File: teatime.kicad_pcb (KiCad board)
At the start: 2 copper layers, 100 x 100 mm, 90 parts, among them J1 PROG, Q1 2N7000, SW1 SW_Push, U1 MCP1700-3302E, U2 74HC595, U3 74HC595, U4 74HC595, U5 74HC595, U6 ATtiny85-20PU

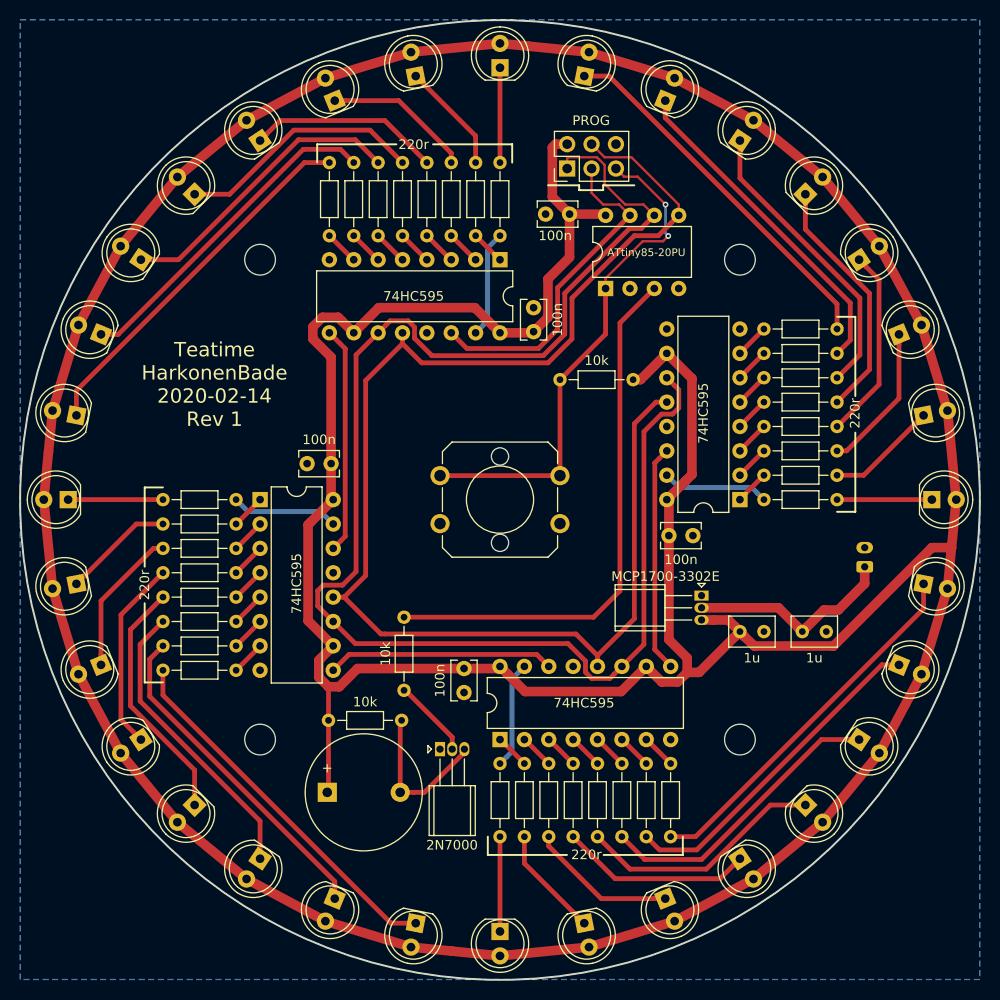
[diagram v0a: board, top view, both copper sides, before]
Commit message: SMD variant board
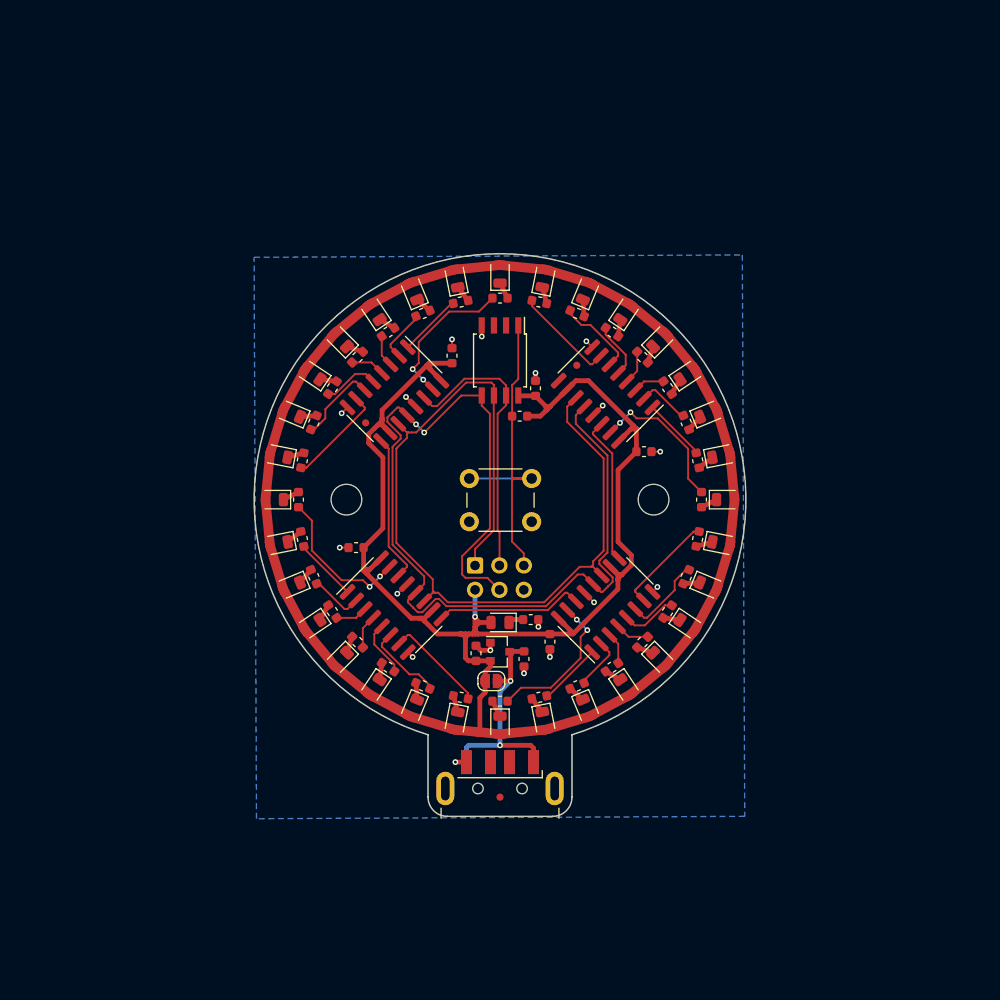
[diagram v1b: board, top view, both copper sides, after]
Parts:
- removed BT1: Battery_Cell, Connector_JST:JST_PH_S2B-PH-K_1x02_P2.00mm_Horizontal
- removed H3, H4: MountingHole, MountingHole:MountingHole_3.2mm_M3
- removed LS1: Speaker, Buzzer_Beeper:Buzzer_12x9.5RM7.6
- removed Q1: 2N7000, Package_TO_SOT_THT:TO-92_Inline_W4.0mm_Horizontal_FlatSideDown
- removed R34: 10k, Resistor_THT:R_Axial_DIN0204_L3.6mm_D1.6mm_P7.62mm_Horizontal
- removed the U3 at (75.0, 100.0)
- added D33: PWR, LED_SMD:LED_0805_2012Metric, F.Cu at (100.0, 112.8)
- added FID1: Fiducial, Fiducial:Fiducial_0.75mm_Mask1.5mm, F.Cu at (100.0, 131.0)
- added FID2: Fiducial, Fiducial:Fiducial_0.75mm_Mask1.5mm, F.Cu at (86.0, 92.0)
- added FID3: Fiducial, Fiducial:Fiducial_0.75mm_Mask1.5mm, F.Cu at (108.0, 86.0)
- added J2: PROG, Connector_IDC:IDC-Header_2x03_P2.54mm_Vertical, B.Cu at (97.4, 106.9)
- added JP1: SolderJumper_2_Open, Jumper:SolderJumper-2_P1.3mm_Open_RoundedPad1.0x1.5mm, F.Cu at (99.1, 118.9)
- added U2: 74HC595, Package_SO:SOIC-16_3.9x9.9mm_P1.27mm, F.Cu at (89.0, 89.0)
- C1, C2: footprint Capacitor_THT:C_Rect_L4.6mm_W3.0mm_P2.50mm_MKS02_FKP02 -> Resistor_SMD:R_0603_1608Metric
- C3, C4, C5, C6, C7: footprint Capacitor_THT:C_Rect_L4.0mm_W2.5mm_P2.50mm -> Resistor_SMD:R_0603_1608Metric
- D1, D10, D11, D12, D13, D14, D15, D16, D17, D18, D19, D2, D20, D21, D22, D23, D24, D25, D26, D27, D28, D29, D3, D30, D31, D32, D4, D5, D6, D7, D8, D9: footprint LED_THT:LED_D5.0mm -> LED_SMD:LED_0805_2012Metric
- J1: value PROG -> USB_A; footprint Connector_PinHeader_2.54mm:PinHeader_2x03_P2.54mm_Vertical -> teatime:USB_A_CNCTech_1001-011-01101_Horizontal_DoubleSided
- R1, R10, R11, R12, R13, R14, R15, R16, R17, R18, R19, R2, R20, R21, R22, R23, R24, R25, R26, R27, R28, R29, R3, R30, R31, R32, R4, R5, R6, R7, R8, R9: value 220r -> 1k; footprint Resistor_THT:R_Axial_DIN0204_L3.6mm_D1.6mm_P7.62mm_Horizontal -> Resistor_SMD:R_0603_1608Metric
- R33: value 10k -> 2k2; footprint Resistor_THT:R_Axial_DIN0204_L3.6mm_D1.6mm_P7.62mm_Horizontal -> Resistor_SMD:R_0603_1608Metric
- R35: footprint Resistor_THT:R_Axial_DIN0204_L3.6mm_D1.6mm_P7.62mm_Horizontal -> Resistor_SMD:R_0603_1608Metric
- SW1: footprint teatime:B3F-40xx -> Button_Switch_THT:SW_PUSH_6mm
- U1: value MCP1700-3302E -> MCP1700-3302E_SOT23; footprint Package_TO_SOT_THT:TO-92_Inline_W4.0mm_Horizontal_FlatSideDown -> Package_TO_SOT_SMD:SOT-23
- U3: renamed from U2; value 74HC595 -> ATtiny45-20SU; footprint Package_DIP:DIP-16_W7.62mm -> Package_SO:SOIJ-8_5.3x5.3mm_P1.27mm
- U4, U5: footprint Package_DIP:DIP-16_W7.62mm -> Package_SO:SOIC-16_3.9x9.9mm_P1.27mm
- U6: value ATtiny85-20PU -> 74HC595; footprint Package_DIP:DIP-8_W7.62mm -> Package_SO:SOIC-16_3.9x9.9mm_P1.27mm
- moved J1 71.8 mm to (100.0, 137.0), turned to 270 degrees
- moved C5 32.6 mm to (115.0, 95.0), turned to 0 degrees
- moved HS1 30.0 mm to (100.0, 86.0)
- moved C1 29.1 mm to (102.5, 116.6), turned to 270 degrees
- moved C4 29.1 mm to (85.0, 105.0), turned to 180 degrees
- moved C2 27.6 mm to (97.5, 116.0), turned to 90 degrees
- moved H1 26.6 mm to (84.0, 100.0)
- moved H2 26.6 mm to (116.0, 100.0)
- moved R33 25.2 mm to (103.2, 112.5)
- moved R35 24.2 mm to (102.0, 91.3), turned to 0 degrees
- moved R32 23.6 mm to (104.1, 79.4), turned to 168.75 degrees
- moved R24 23.6 mm to (120.6, 104.1), turned to 78.75 degrees
- moved R8 23.6 mm to (79.4, 95.9), turned to 258.75 degrees
- moved R16 23.6 mm to (95.9, 120.6), turned to 348.75 degrees
- moved U1 21.8 mm to (100.0, 115.8), turned to 0 degrees
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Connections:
- C1 pad 1: Net-(BT1-Pad1) -> Net-(C1-Pad1)
- J1 pad 1: Net-(J1-Pad1) -> Net-(C1-Pad1)
- J1 pad 2: +3V3 -> Net-(J1-Pad2)
- J1 pad 4: Net-(J1-Pad4) -> GND
- J1 pad 5: Net-(J1-Pad5) -> GND
- R1 pad 1: Net-(R1-Pad1) -> Net-(D1-Pad1)
- R1 pad 2: Net-(D1-Pad1) -> Net-(R1-Pad2)
- R10 pad 1: Net-(R10-Pad1) -> Net-(D10-Pad1)
- R10 pad 2: Net-(D10-Pad1) -> Net-(R10-Pad2)
- R11 pad 1: Net-(R11-Pad1) -> Net-(D11-Pad1)
- R11 pad 2: Net-(D11-Pad1) -> Net-(R11-Pad2)
- R12 pad 1: Net-(R12-Pad1) -> Net-(D12-Pad1)
- R12 pad 2: Net-(D12-Pad1) -> Net-(R12-Pad2)
- R13 pad 1: Net-(R13-Pad1) -> Net-(D13-Pad1)
- R13 pad 2: Net-(D13-Pad1) -> Net-(R13-Pad2)
- R14 pad 1: Net-(R14-Pad1) -> Net-(D14-Pad1)
- R14 pad 2: Net-(D14-Pad1) -> Net-(R14-Pad2)
- R15 pad 1: Net-(R15-Pad1) -> Net-(D15-Pad1)
- R15 pad 2: Net-(D15-Pad1) -> Net-(R15-Pad2)
- R16 pad 1: Net-(R16-Pad1) -> Net-(D16-Pad1)
- R16 pad 2: Net-(D16-Pad1) -> Net-(R16-Pad2)
- R17 pad 1: Net-(R17-Pad1) -> Net-(D17-Pad1)
- R17 pad 2: Net-(D17-Pad1) -> Net-(R17-Pad2)
- R18 pad 1: Net-(R18-Pad1) -> Net-(D18-Pad1)
- R18 pad 2: Net-(D18-Pad1) -> Net-(R18-Pad2)
- R19 pad 1: Net-(R19-Pad1) -> Net-(D19-Pad1)
- R19 pad 2: Net-(D19-Pad1) -> Net-(R19-Pad2)
- R2 pad 1: Net-(R2-Pad1) -> Net-(D2-Pad1)
- R2 pad 2: Net-(D2-Pad1) -> Net-(R2-Pad2)
- R20 pad 1: Net-(R20-Pad1) -> Net-(D20-Pad1)
- R20 pad 2: Net-(D20-Pad1) -> Net-(R20-Pad2)
- R21 pad 1: Net-(R21-Pad1) -> Net-(D21-Pad1)
- R21 pad 2: Net-(D21-Pad1) -> Net-(R21-Pad2)
- R22 pad 1: Net-(R22-Pad1) -> Net-(D22-Pad1)
- R22 pad 2: Net-(D22-Pad1) -> Net-(R22-Pad2)
- R23 pad 1: Net-(R23-Pad1) -> Net-(D23-Pad1)
- R23 pad 2: Net-(D23-Pad1) -> Net-(R23-Pad2)
- R24 pad 1: Net-(R24-Pad1) -> Net-(D24-Pad1)
- R24 pad 2: Net-(D24-Pad1) -> Net-(R24-Pad2)
- R25 pad 1: Net-(R25-Pad1) -> Net-(D25-Pad1)
- R25 pad 2: Net-(D25-Pad1) -> Net-(R25-Pad2)
- R26 pad 1: Net-(R26-Pad1) -> Net-(D26-Pad1)
- R26 pad 2: Net-(D26-Pad1) -> Net-(R26-Pad2)
- R27 pad 1: Net-(R27-Pad1) -> Net-(D27-Pad1)
- R27 pad 2: Net-(D27-Pad1) -> Net-(R27-Pad2)
- R28 pad 1: Net-(R28-Pad1) -> Net-(D28-Pad1)
- R28 pad 2: Net-(D28-Pad1) -> Net-(R28-Pad2)
- R29 pad 1: Net-(R29-Pad1) -> Net-(D29-Pad1)
- R29 pad 2: Net-(D29-Pad1) -> Net-(R29-Pad2)
- R3 pad 1: Net-(R3-Pad1) -> Net-(D3-Pad1)
- R3 pad 2: Net-(D3-Pad1) -> Net-(R3-Pad2)
- R30 pad 1: Net-(R30-Pad1) -> Net-(D30-Pad1)
- R30 pad 2: Net-(D30-Pad1) -> Net-(R30-Pad2)
- R31 pad 1: Net-(R31-Pad1) -> Net-(D31-Pad1)
- R31 pad 2: Net-(D31-Pad1) -> Net-(R31-Pad2)
- R32 pad 1: Net-(R32-Pad1) -> Net-(D32-Pad1)
- R32 pad 2: Net-(D32-Pad1) -> Net-(R32-Pad2)
- R33 pad 1: Net-(J1-Pad5) -> Net-(D33-Pad1)
- R33 pad 2: +3V3 -> GND
- R35 pad 1: Net-(R35-Pad1) -> Net-(J2-Pad5)
- R35 pad 2: Net-(Q1-Pad2) -> +3V3
- R4 pad 1: Net-(R4-Pad1) -> Net-(D4-Pad1)
- R4 pad 2: Net-(D4-Pad1) -> Net-(R4-Pad2)
- R5 pad 1: Net-(R5-Pad1) -> Net-(D5-Pad1)
- R5 pad 2: Net-(D5-Pad1) -> Net-(R5-Pad2)
- R6 pad 1: Net-(R6-Pad1) -> Net-(D6-Pad1)
- R6 pad 2: Net-(D6-Pad1) -> Net-(R6-Pad2)
- R7 pad 1: Net-(R7-Pad1) -> Net-(D7-Pad1)
- R7 pad 2: Net-(D7-Pad1) -> Net-(R7-Pad2)
- R8 pad 1: Net-(R8-Pad1) -> Net-(D8-Pad1)
- R8 pad 2: Net-(D8-Pad1) -> Net-(R8-Pad2)
- R9 pad 1: Net-(R9-Pad1) -> Net-(D9-Pad1)
- R9 pad 2: Net-(D9-Pad1) -> Net-(R9-Pad2)
- SW1 pad 1: Net-(J1-Pad5) -> Net-(J2-Pad5)
- U1 pad 2: Net-(BT1-Pad1) -> +3V3
- U1 pad 3: +3V3 -> Net-(C1-Pad1)
- U3 pad 1: Net-(R2-Pad1) -> Net-(J2-Pad5)
- U3 pad 2: Net-(R3-Pad1) -> Net-(U3-Pad2)
- U3 pad 3: Net-(R4-Pad1) -> Net-(U3-Pad3)
- U3 pad 4: Net-(R5-Pad1) -> GND
- U3 pad 5: Net-(R6-Pad1) -> Net-(J2-Pad4)
- U3 pad 6: Net-(R7-Pad1) -> Net-(J2-Pad1)
- U3 pad 7: Net-(R8-Pad1) -> Net-(J2-Pad3)
- U3 pad 8: GND -> +3V3
- U4 pad 1: Net-(R18-Pad1) -> Net-(R10-Pad2)
- U4 pad 11: Net-(J1-Pad1) -> Net-(J2-Pad1)
- U4 pad 12: Net-(J1-Pad4) -> Net-(J2-Pad4)
- U4 pad 15: Net-(R17-Pad1) -> Net-(R9-Pad2)
- U4 pad 2: Net-(R19-Pad1) -> Net-(R11-Pad2)
- U4 pad 3: Net-(R20-Pad1) -> Net-(R12-Pad2)
- U4 pad 4: Net-(R21-Pad1) -> Net-(R13-Pad2)
- U4 pad 5: Net-(R22-Pad1) -> Net-(R14-Pad2)
- U4 pad 6: Net-(R23-Pad1) -> Net-(R15-Pad2)
- U4 pad 7: Net-(R24-Pad1) -> Net-(R16-Pad2)
- U5 pad 1: Net-(R26-Pad1) -> Net-(R18-Pad2)
- U5 pad 11: Net-(J1-Pad1) -> Net-(J2-Pad1)
- U5 pad 12: Net-(J1-Pad4) -> Net-(J2-Pad4)
- U5 pad 15: Net-(R25-Pad1) -> Net-(R17-Pad2)
- U5 pad 2: Net-(R27-Pad1) -> Net-(R19-Pad2)
- U5 pad 3: Net-(R28-Pad1) -> Net-(R20-Pad2)
- U5 pad 4: Net-(R29-Pad1) -> Net-(R21-Pad2)
- U5 pad 5: Net-(R30-Pad1) -> Net-(R22-Pad2)
- U5 pad 6: Net-(R31-Pad1) -> Net-(R23-Pad2)
- U5 pad 7: Net-(R32-Pad1) -> Net-(R24-Pad2)
- U6 pad 1: Net-(J1-Pad5) -> Net-(R26-Pad2)
- U6 pad 2: Net-(U6-Pad2) -> Net-(R27-Pad2)
- U6 pad 3: Net-(R35-Pad1) -> Net-(R28-Pad2)
- U6 pad 4: GND -> Net-(R29-Pad2)
- U6 pad 5: Net-(J1-Pad4) -> Net-(R30-Pad2)
- U6 pad 6: Net-(J1-Pad1) -> Net-(R31-Pad2)
- U6 pad 7: Net-(J1-Pad3) -> Net-(R32-Pad2)
- U6 pad 8: +3V3 -> GND
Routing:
- net +3V3: track 525.5 -> 291.9 mm, vias 0 -> 1
- net Net-(J1-Pad1): track 155.9 -> 0.00 mm
- net Net-(J1-Pad4): track 142.6 -> 0.00 mm
- net Net-(J2-Pad4): track 0.00 -> 106.1 mm, vias 0 -> 2
- net Net-(J2-Pad1): track 0.00 -> 92.9 mm
- net Net-(R35-Pad1): track 56.6 -> 0.00 mm
- net Net-(J1-Pad5): track 53.5 -> 0.00 mm, vias 2 -> 0
- net Net-(D8-Pad1): track 38.8 -> 1.75 mm
- net Net-(D32-Pad1): track 38.8 -> 1.75 mm
- net Net-(D24-Pad1): track 38.8 -> 1.75 mm
- net Net-(D16-Pad1): track 38.8 -> 1.75 mm
- net Net-(J1-Pad3): track 35.1 -> 0.00 mm
- net Net-(J2-Pad5): track 0.00 -> 34.8 mm
- net Net-(D15-Pad1): track 34.9 -> 1.75 mm
- net Net-(D7-Pad1): track 34.9 -> 1.75 mm
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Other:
- board size 100 x 100 mm -> 51.2 x 58.6 mm
- board text added: "Teatime - SMD HarkonenBade 2020-09-12 Rev 1"
- board text removed: "+"
- board text removed: "-"
- board text removed: "Lithium Primary 3.5V Min"
- board text removed: "Teatime HarkonenBade 2020-02-14 Rev 1"

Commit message: Completed board
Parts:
- removed HS1: QR, teatime:__github.com_HarkonenBade_teatime
- added LS1: Speaker, Buzzer_Beeper:Buzzer_15x7.5RM7.6, B.Cu at (103.9, 95.0)
- added Q1: 2N7002, Package_TO_SOT_SMD:SOT-23, F.Cu at (107.0, 101.0)
- added R34: 10k, Resistor_SMD:R_0603_1608Metric, F.Cu at (106.0, 95.7)
- added R36: 10k, Resistor_SMD:R_0603_1608Metric, F.Cu at (106.8, 98.2)
- J2: footprint Connector_IDC:IDC-Header_2x03_P2.54mm_Vertical -> Connector_PinHeader_2.54mm:PinHeader_2x03_P2.54mm_Vertical; moved to F.Cu
- U1: value MCP1700-3302E_SOT23 -> MCP1700-3302
- moved R33 6.40 mm to (96.8, 112.8), turned to 180 degrees
- moved J2 5.21 mm to (102.5, 106.0)
- turned D33 to 0 degrees
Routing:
- net Net-(R36-Pad2): track 0.00 -> 24.3 mm, vias 0 -> 2
- net Net-(LS1-Pad2): track 0.00 -> 15.5 mm, vias 0 -> 1
- net +3V3: track 291.9 -> 298.0 mm
- net Net-(J2-Pad4): track 106.1 -> 101.5 mm
- net GND: track 19.4 -> 22.5 mm
- net Net-(J2-Pad5): track 34.8 -> 36.7 mm, vias 0 -> 1
- net Net-(Q1-Pad1): track 0.00 -> 1.80 mm
- net Net-(J2-Pad1): track 92.9 -> 93.9 mm, vias 0 -> 1
- net Net-(J2-Pad3): track 29.6 -> 28.5 mm
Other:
- board text added: "Teatime - SMD HarkonenBade 2020-09-17 Rev 1"
- board text removed: "Teatime - SMD HarkonenBade 2020-09-12 Rev 1"

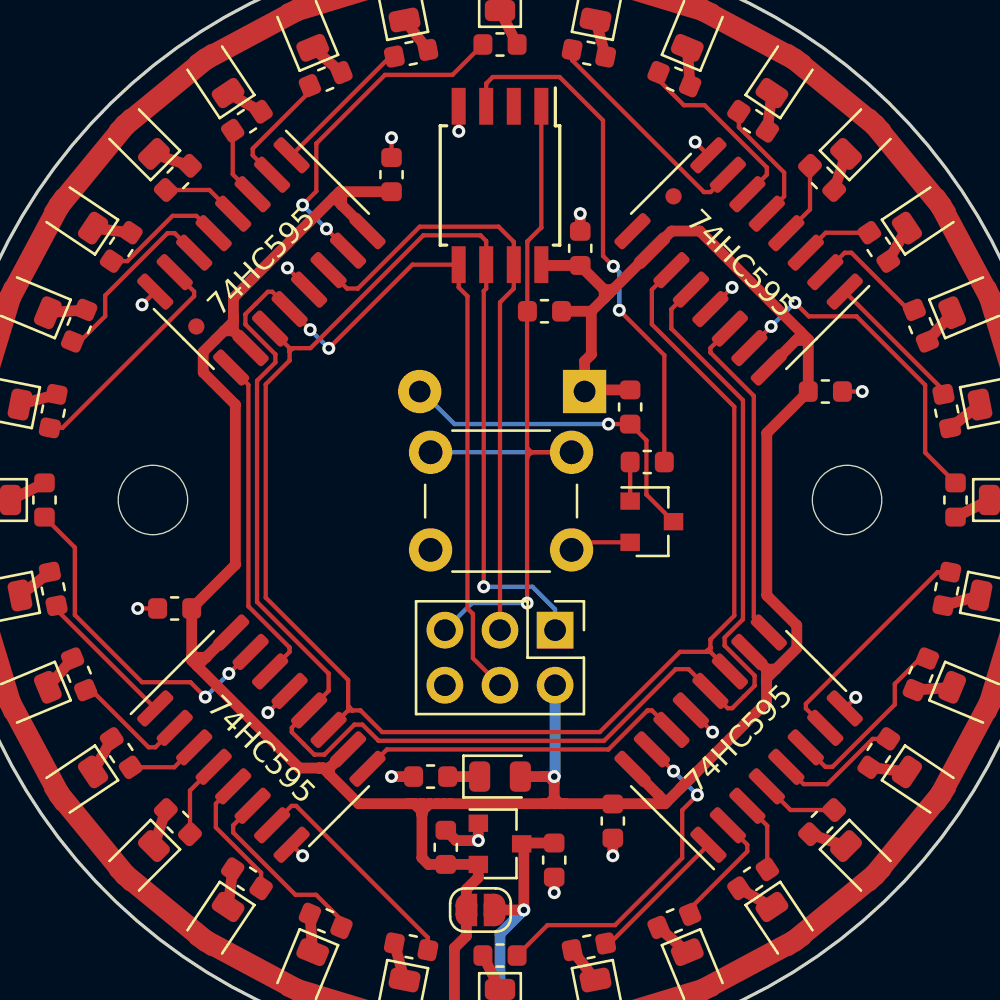
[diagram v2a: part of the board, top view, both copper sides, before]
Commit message: Cant decoupling caps over
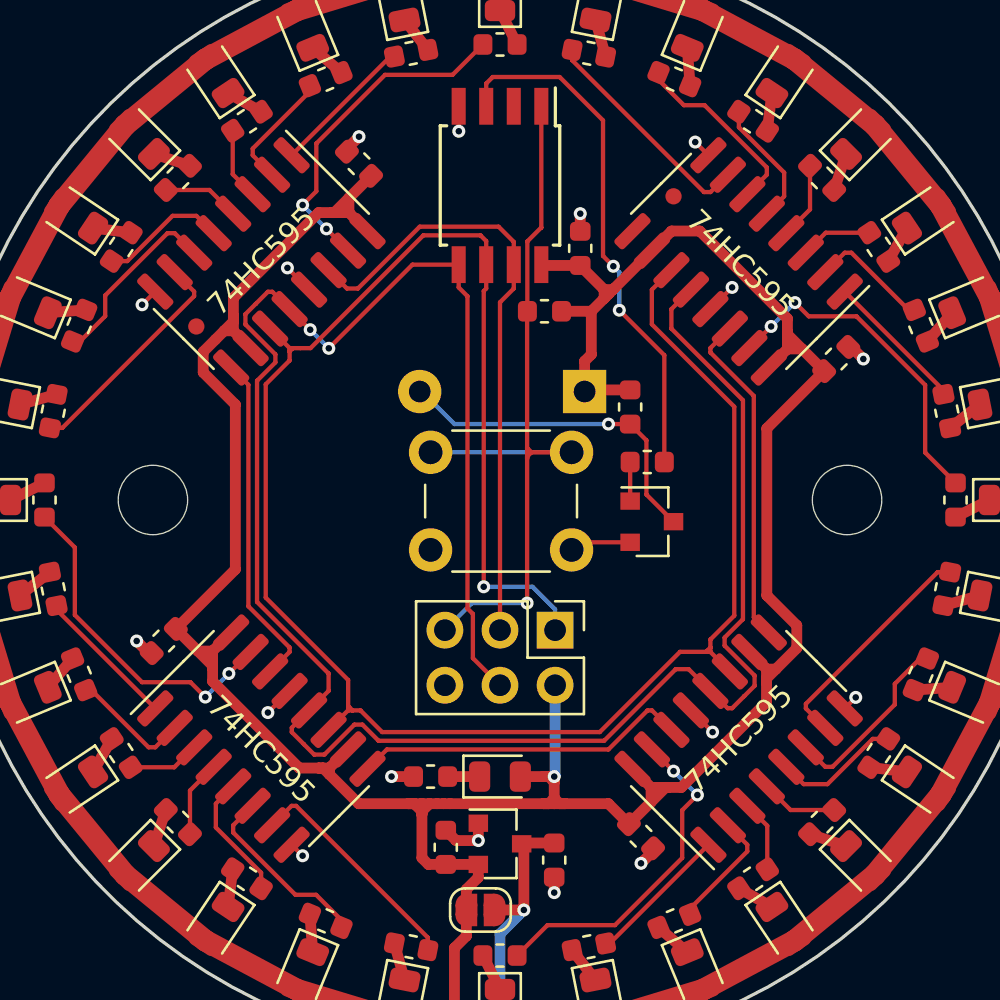
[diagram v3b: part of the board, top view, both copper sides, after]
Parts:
- C1, C2, C3, C4, C5, C6, C7: footprint Resistor_SMD:R_0603_1608Metric -> Capacitor_SMD:C_0603_1608Metric
- U1: value MCP1700-3302 -> MCP1700-3302E_SOT23
- moved C3 1.58 mm to (93.5, 84.5), turned to 135 degrees
- moved C4 1.58 mm to (84.5, 106.5), turned to 225 degrees
- moved C5 1.58 mm to (115.5, 93.5), turned to 45 degrees
- moved C6 1.48 mm to (106.5, 115.5), turned to 315 degrees
